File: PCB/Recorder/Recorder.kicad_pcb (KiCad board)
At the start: 2 copper layers, 70 x 70 mm, 54 parts, among them J1 Battery, J2 Reset, J3 TC2030-USB-NL-DS, J4 TF_PUSH, J5 USB-C-Socket-H, Q2 CJ2301, SW1 SW_Push, U1 R, U2 L, U3 TP4054, U4 ME6211C33M5G-N, U5 MAX98357A, U6 ESP32-S3-MINI-1

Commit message: Tidy SS
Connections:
- net BLINK2 renamed LEDMIC
- U6 pad 14: SCK -> unconnected-(U6-GPIO10-Pad14)
- U6 pad 9: unconnected-(U6-GPIO5-Pad9) -> SCK
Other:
- board text added: "12 13 14 15 17 5 6 7"
- board text added: "35 36 37 38"
- board text added: "MIC"
- board text added: "SPK"
- board text added: "SS MOSI SCK MISO CD C W D"
- board text added: "W C D P"
- board text removed: "12 13 14 15 17 6 7 10"
- board text removed: "SS MOSI SCK MISO CD WS SD SCK"

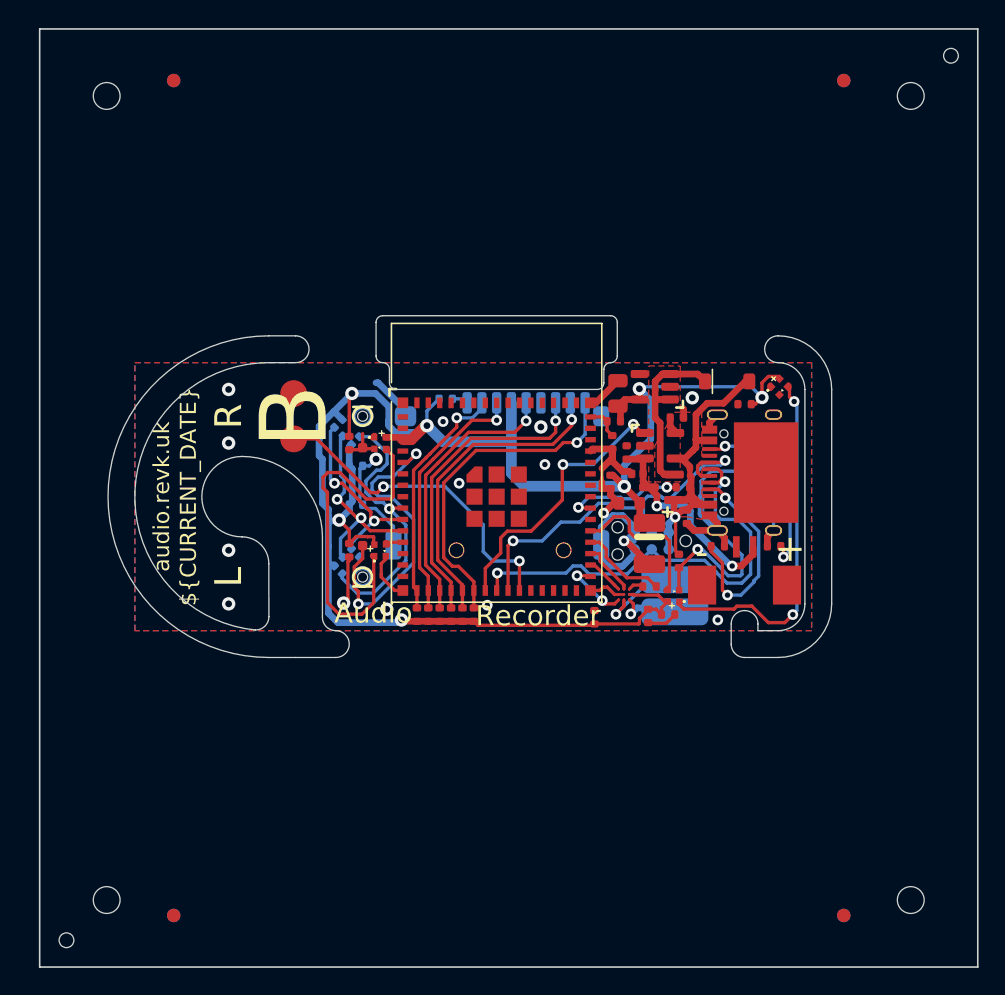
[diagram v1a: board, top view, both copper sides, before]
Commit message: Fix component size
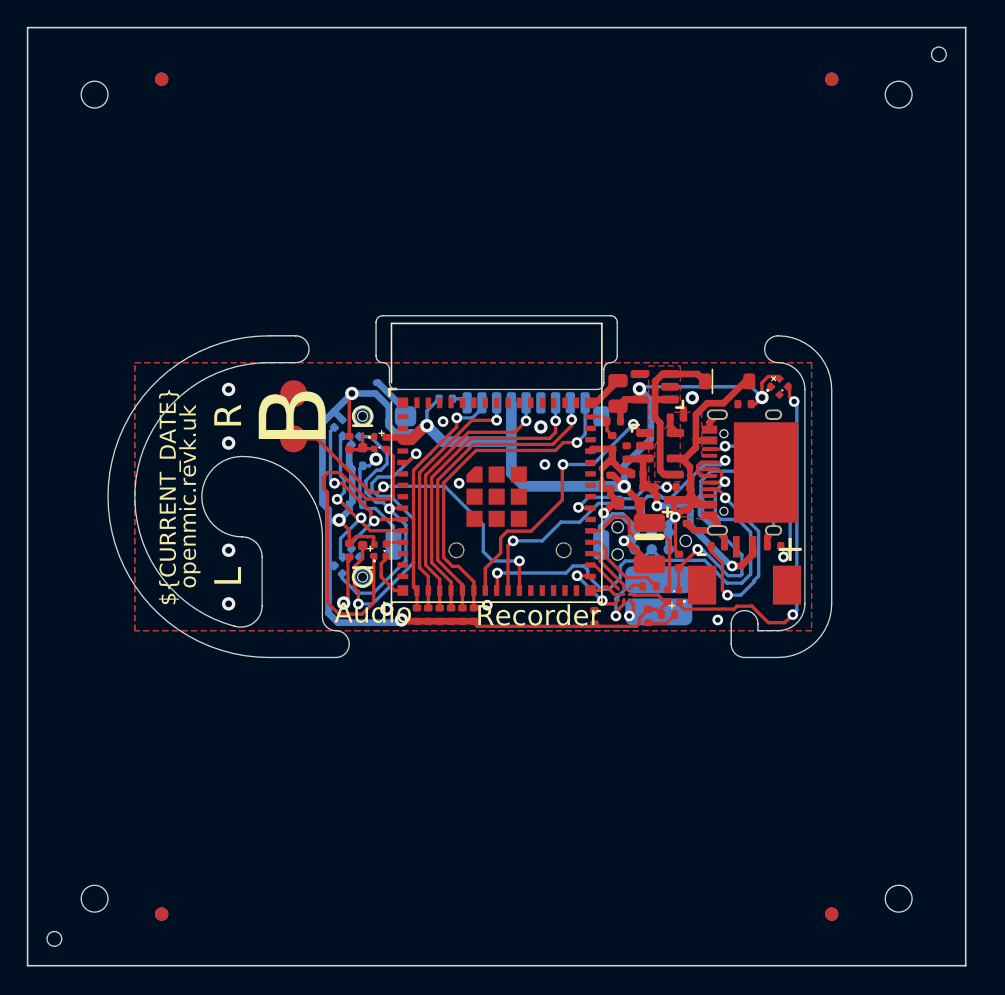
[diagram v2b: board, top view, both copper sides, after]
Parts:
- moved TP1 1.20 mm to (112.1, 108.6)
- moved TP2 1.20 mm to (112.1, 106.2)
- moved PCB1 0.91 mm to (100.0, 100.0)
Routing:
- net GND: track 90.2 -> 85.7 mm
- net Net-(U5-OUTP): track 4.31 -> 1.02 mm
- net D-: track 35.6 -> 37.3 mm
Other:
- board text added: "12 13 14 15 17"
- board text added: "35 36"
- board text added: "37 38"
- board text added: "5 6 7"
- board text added: "C W D"
- board text added: "D P"
- board text added: "SS MOSI SCK MISO CD"
- board text added: "W C"
- board text added: "openmic.revk.uk"
- board text removed: "12 13 14 15 17 5 6 7"
- board text removed: "35 36 37 38"
- board text removed: "SS MOSI SCK MISO CD C W D"
- board text removed: "W C D P"
- board text removed: "audio.revk.uk"
